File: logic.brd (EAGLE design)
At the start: 37.4 x 32.5 mm, 10 parts, among them CON1 PINHEAD_1X10-2, CON2 PINHEAD_1X10-2, CON3 PINHEAD_1X02-2, CON4 PINHEAD_1X02-2, CON5 PINHEAD_1X02-2, CON6 PINHEAD_1X02-2, CON7 PINHEAD_1X07-2

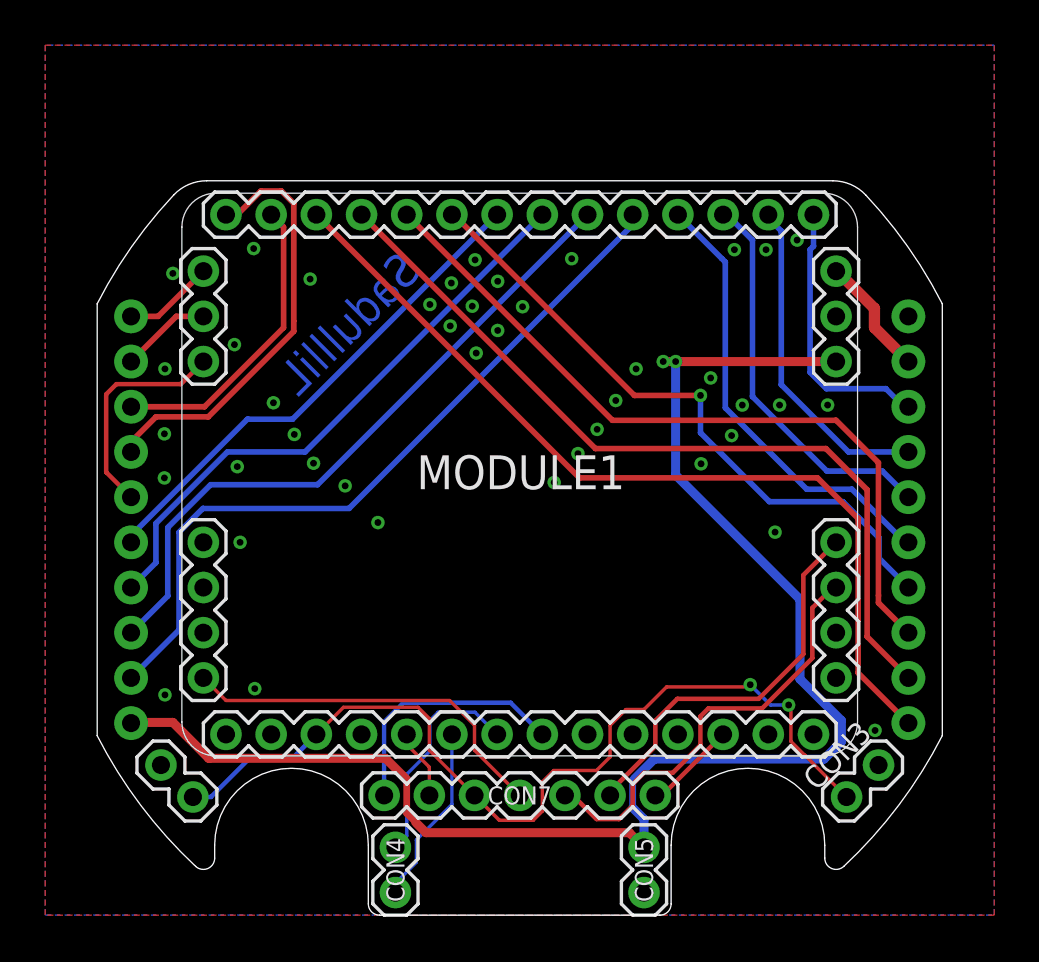
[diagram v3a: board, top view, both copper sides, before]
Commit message: fixed logic board to fit housing  better
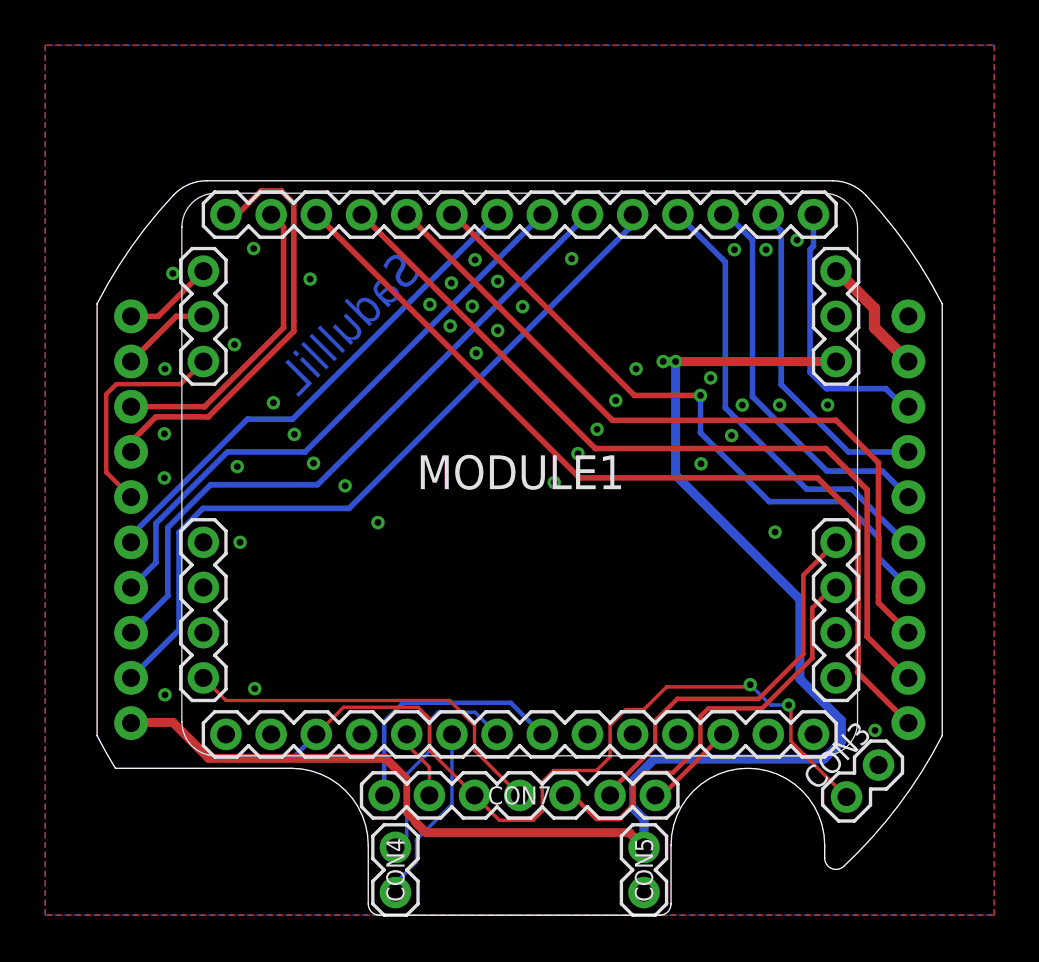
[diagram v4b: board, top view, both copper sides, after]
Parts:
- removed CON6: PINHEAD_1X02-2, pinhead:1X02-PTH-2
- added U$4: (no value), logo:DRAGON-18X7
- MODULE1: device zubax_modules:MITOHONDRIQUE -> zubax_modules:MITOHONDRIQUE-TH
- moved U$2 6.94 mm to (12.4, -7.70)
- moved U$1 1.40 mm to (6.22, 5.95)
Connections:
- net GND: no longer CON6.2
- net GPIO1: no longer CON6.1
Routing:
- net GPIO1: track 40.5 -> 37.3 mm
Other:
- outline, holes or cut-outs redrawn
